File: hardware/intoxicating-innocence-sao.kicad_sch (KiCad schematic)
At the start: 0 parts

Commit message: Create board schematic
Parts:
- added C1: 100nF, Capacitor_SMD:C_0603_1608Metric_Pad1.08x0.95mm_HandSolder, symbol Device:C
- added D1, D2, D3: RED, LED_THT:LED_D3.0mm, symbol Device:LED
- added J1: SAO, kantoniak-kicad:SAO_Header_Addon_Side, symbol kantoniak-kicad:Conn_SAO
- added J2: QWIIC, Connector_JST:JST_SH_SM04B-SRSS-TB_1x04-1MP_P1.00mm_Horizontal, symbol kantoniak-kicad:QWIIC
- added R1, R10, R2, R8, R9: 10k, Resistor_SMD:R_0603_1608Metric_Pad0.98x0.95mm_HandSolder, symbol Device:R
- added R3, R4, R5, R6, R7: 330, Resistor_SMD:R_0603_1608Metric_Pad0.98x0.95mm_HandSolder, symbol Device:R
- added TP1: 3V3, TestPoint:TestPoint_Pad_D1.5mm, symbol Connector:TestPoint
- added TP2: GND, TestPoint:TestPoint_Pad_D1.5mm, symbol Connector:TestPoint
- added TP3: SWIO, TestPoint:TestPoint_Pad_D1.5mm, symbol Connector:TestPoint
- added TP4: ~{RST}, TestPoint:TestPoint_Pad_D1.5mm, symbol Connector:TestPoint
- added TP5: TXD, TestPoint:TestPoint_Pad_D1.5mm, symbol Connector:TestPoint
- added TP6: RXD, TestPoint:TestPoint_Pad_D1.5mm, symbol Connector:TestPoint
- added U1: CH32V003F4P6, Package_SO:TSSOP-20_4.4x6.5mm_P0.65mm, symbol MCU_WCH_RiscV:CH32V003FxPx
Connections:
- new net: D1.2 (A), R5.1
- new net: D2.2 (A), R6.1
- new net: D3.2 (A), R7.1
- new net: R4.2, U1.3 (PD6)
- new net: R3.1, U1.2 (PD5)
- new net +3V3: C1.1, J1.6 (3V3), J2.2 (3V3), R1.2, R2.2, TP1.1, U1.9 (VDD)
- new net CONFIG_A: R8.1, U1.17 (PC7)
- new net CONFIG_B: R9.2, U1.19 (PD2)
- new net CONFIG_C: R10.2, U1.20 (PD3)
- new net GND: C1.2, D1.1 (K), D2.1 (K), D3.1 (K), J1.1 (GND), J2.1 (GND), R10.1, R8.2, R9.1, TP2.1, U1.7 (VSS)
- new net LED_LEFT: R5.2, U1.13 (PC3)
- new net LED_RIGHT: R6.2, U1.14 (PC4)
- new net LED_TOP: R7.2, U1.15 (PC5)
- new net SCL: J1.2 (SCL), J2.3 (SDA), R2.1, U1.12 (PC2)
- new net SDA: J1.5 (SDA), J2.4 (SCL), R1.1, U1.11 (PC1)
- new net SWIO: TP3.1, U1.18 (PD1)
- new net UART_RX: R4.1, TP6.1
- new net UART_TX: R3.2, TP5.1
- new net ~{RST}: TP4.1, U1.4 (PD7)
- no-connect marks 0 -> 8
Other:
- note added: "Connectors"
- note added: "Extra configuration"
- note added: "LEDs - Eyes"

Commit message: Add bulk capacitor
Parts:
- added C1: 10uF, Capacitor_SMD:C_0603_1608Metric_Pad1.08x0.95mm_HandSolder, symbol Device:C
- renumbered C1 to C2
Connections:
- net +3V3: now also C1.1
- net GND: now also C1.2
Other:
- moved on the sheet: C2
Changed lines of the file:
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@@
 	)
 	(junction
+		(at 72.39 53.34)
+		(diameter 0)
+		(color 0 0 0 0)
+	)
+	(junction
 		(at 200.66 43.18)
 		(diameter 0)
@@
 	)
 	(junction
-		(at 82.55 30.48)
+		(at 81.28 30.48)
+		(diameter 0)
+		(color 0 0 0 0)
+	)
+	(junction
+		(at 72.39 30.48)
 		(diameter 0)
 		(color 0 0 0 0)
 	)
 	(junction
-		(at 82.55 53.34)
+		(at 81.28 53.34)
 		(diameter 0)
 		(color 0 0 0 0)
@@
 	(wire
 		(pts
+			(xy 72.39 30.48) (xy 72.39 38.1)
+		)
+		(stroke
+			(width 0)
+			(type default)
+		)
+	)
+	(wire
+		(pts
 			(xy 110.49 57.15) (xy 120.65 57.15)
 		)
@@
 	(wire
 		(pts
+			(xy 72.39 30.48) (xy 90.17 30.48)
+		)
+		(stroke
+			(width 0)
+			(type default)
+		)
+	)
+	(wire
+		(pts
 			(xy 45.72 48.26) (xy 45.72 53.34)
 		)
@@
 	(wire
 		(pts
-			(xy 82.55 53.34) (xy 82.55 55.88)
+			(xy 81.28 53.34) (xy 81.28 55.88)
 		)
 		(stroke
@@
 	(wire
 		(pts
-			(xy 82.55 30.48) (xy 82.55 38.1)
+			(xy 90.17 30.48) (xy 90.17 38.1)
 		)
 		(stroke
@@
 	(wire
 		(pts
-			(xy 41.91 40.64) (xy 59.69 40.64)
+			(xy 41.91 40.64) (xy 49.53 40.64)
+		)
+		(stroke
+			(width 0)
+			(type default)
+		)
+	)
+	(wire
+		(pts
+			(xy 41.91 38.1) (xy 49.53 38.1)
 		)
 		(stroke
@@
 	(wire
 		(pts
-			(xy 41.91 38.1) (xy 59.69 38.1)
+			(xy 72.39 53.34) (xy 90.17 53.34)
 		)
 		(stroke
@@
 	(wire
 		(pts
-			(xy 82.55 53.34) (xy 45.72 53.34)
+			(xy 72.39 45.72) (xy 72.39 53.34)
+		)
+		(stroke
+			(width 0)
+			(type default)
+		)
+	)
+	(wire
+		(pts
+			(xy 45.72 53.34) (xy 72.39 53.34)
 		)
 		(stroke
@@
 	(wire
 		(pts
-			(xy 82.55 27.94) (xy 82.55 30.48)
+			(xy 81.28 27.94) (xy 81.28 30.48)
 		)
 		(stroke
@@
 	(wire
 		(pts
-			(xy 45.72 30.48) (xy 82.55 30.48)
+			(xy 45.72 30.48) (xy 72.39 30.48)
 		)
 		(stroke
@@
 	(wire
 		(pts
-			(xy 82.55 45.72) (xy 82.55 53.34)
+			(xy 90.17 45.72) (xy 90.17 53.34)
 		)
 		(stroke
@@
 	(global_label "SDA"
 		(shape bidirectional)
-		(at 59.69 40.64 0)
+		(at 49.53 40.64 0)
 		(fields_autoplaced yes)
 		(effects
@@
 		)
 		(property "Intersheetrefs" "${INTERSHEET_REFS}"
-			(at 67.3546 40.64 0)
+			(at 57.1946 40.64 0)
 			(hide yes)
 			(show_name no)
@@
 	(global_label "SCL"
 		(shape output)
-		(at 59.69 38.1 0)
+		(at 49.53 38.1 0)
 		(fields_autoplaced yes)
 		(effects
@@
 		)
 		(property "Intersheetrefs" "${INTERSHEET_REFS}"
-			(at 66.1828 38.1 0)
+			(at 56.0228 38.1 0)
 			(hide yes)
 			(show_name no)
@@
 	)
 	(symbol
+		(lib_id "Device:C")
+		(at 72.39 41.91 0)
+		(unit 1)
+		(body_style 1)
+		(exclude_from_sim no)
+		(in_bom yes)
+		(on_board yes)
+		(in_pos_files yes)
+		(dnp no)
+		(fields_autoplaced yes)
+		(property "Reference" "C1"
+			(at 76.2 40.6399 0)
+			(show_name no)
+			(do_not_autoplace no)
+			(effects
+				(font
+					(size 1.27 1.27)
+				)
+				(justify left)
+			)
+		)
+		(property "Value" "10uF"
+			(at 76.2 43.1799 0)
+			(show_name no)
+			(do_not_autoplace no)
+			(effects
+				(font
+					(size 1.27 1.27)
+				)
+				(justify left)
+			)
+		)
+		(property "Footprint" "Capacitor_SMD:C_0603_1608Metric_Pad1.08x0.95mm_HandSolder"
+			(at 73.3552 45.72 0)
+			(hide yes)
+			(show_name no)
+			(do_not_autoplace no)
+			(effects
+				(font
+					(size 1.27 1.27)
+				)
+			)
+		)
+		(property "Datasheet" ""
+			(at 72.39 41.91 0)
+			(hide yes)
+			(show_name no)
+			(do_not_autoplace no)
+			(effects
+				(font
+					(size 1.27 1.27)
+				)
+			)
+		)
+		(property "Description" "Unpolarized capacitor"
+			(at 72.39 41.91 0)
+			(hide yes)
+			(show_name no)
+			(do_not_autoplace no)
+			(effects
+				(font
+					(size 1.27 1.27)
+				)
+			)
+		)
+		(property "LCSC Part #" "C109455"
+			(at 72.39 41.91 0)
+			(hide yes)
+			(show_name no)
+			(do_not_autoplace no)
+			(effects
+				(font
+					(size 1.27 1.27)
+				)
+			)
+		)
+		(pin "1"
+		)
+		(pin "2"
+		)
+		(instances
+			(project "intoxicating-innocence-sao"
+				(path "/559a265e-8809-44d3-9227-9bc29ae1c837"
+					(reference "C1")
+					(unit 1)
+				)
+			)
+		)
+	)
+	(symbol
 		(lib_id "Device:R")
 		(at 250.19 35.56 90)
@@
 	(symbol
 		(lib_id "Device:C")
-		(at 82.55 41.91 0)
+		(at 90.17 41.91 0)
 		(unit 1)
 		(body_style 1)
@@
 		(dnp no)
 		(fields_autoplaced yes)
-		(property "Reference" "C1"
-			(at 86.36 40.6399 0)
+		(property "Reference" "C2"
+			(at 93.98 40.6399 0)
 			(show_name no)
 			(do_not_autoplace no)
@@
 		)
 		(property "Value" "100nF"
-			(at 86.36 43.1799 0)
+			(at 93.98 43.1799 0)
 			(show_name no)
 			(do_not_autoplace no)
@@
 		)
 		(property "Footprint" "Capacitor_SMD:C_0603_1608Metric_Pad1.08x0.95mm_HandSolder"
-			(at 83.5152 45.72 0)
+			(at 91.1352 45.72 0)
 			(hide yes)
 			(show_name no)
@@
 		)
 		(property "Datasheet" ""
-			(at 82.55 41.91 0)
+			(at 90.17 41.91 0)
 			(hide yes)
 			(show_name no)
@@
 		)
 		(property "Description" "Unpolarized capacitor"
-			(at 82.55 41.91 0)
+			(at 90.17 41.91 0)
 			(hide yes)
 			(show_name no)
@@
 		)
 		(property "LCSC Part #" "C14663"
-			(at 82.55 41.91 0)
+			(at 90.17 41.91 0)
 			(hide yes)
 			(show_name no)
@@
 			(project "intoxicating-innocence-sao"
 				(path "/559a265e-8809-44d3-9227-9bc29ae1c837"
-					(reference "C1")
+					(reference "C2")
 					(unit 1)
 				)
@@
 	(symbol
 		(lib_id "power:+3V3")
-		(at 82.55 27.94 0)
+		(at 81.28 27.94 0)
 		(unit 1)
 		(body_style 1)
@@
 		(fields_autoplaced yes)
 		(property "Reference" "#PWR03"
-			(at 82.55 31.75 0)
+			(at 81.28 31.75 0)
 			(hide yes)
 			(show_name no)
@@
 		)
 		(property "Value" "+3V3"
-			(at 85.09 26.6699 0)
+			(at 83.82 26.6699 0)
 			(show_name no)
 			(do_not_autoplace no)
@@
 		)
 		(property "Footprint" ""
-			(at 82.55 27.94 0)
+			(at 81.28 27.94 0)
 			(hide yes)
 			(show_name no)
@@
 		)
 		(property "Datasheet" ""
-			(at 82.55 27.94 0)
+			(at 81.28 27.94 0)
 			(hide yes)
 			(show_name no)
@@
 		)
 		(property "Description" "Power symbol creates a global label with name \"+3V3\""
-			(at 82.55 27.94 0)
+			(at 81.28 27.94 0)
 			(hide yes)
 			(show_name no)
@@
 	(symbol
 		(lib_id "power:GND")
-		(at 82.55 55.88 0)
+		(at 81.28 55.88 0)
 		(unit 1)
 		(body_style 1)
@@
 		(fields_autoplaced yes)
 		(property "Reference" "#PWR04"
-			(at 82.55 62.23 0)
+			(at 81.28 62.23 0)
 			(hide yes)
 			(show_name no)
@@
 		)
 		(property "Value" "GND"
-			(at 85.09 57.1499 0)
+			(at 83.82 57.1499 0)
 			(show_name no)
 			(do_not_autoplace no)
@@
 		)
 		(property "Footprint" ""
-			(at 82.55 55.88 0)
+			(at 81.28 55.88 0)
 			(hide yes)
 			(show_name no)
@@
 		)
 		(property "Datasheet" ""
-			(at 82.55 55.88 0)
+			(at 81.28 55.88 0)
 			(hide yes)
 			(show_name no)
@@
 		)
 		(property "Description" "Power symbol creates a global label with name \"GND\" , ground"
-			(at 82.55 55.88 0)
+			(at 81.28 55.88 0)
 			(hide yes)
 			(show_name no)

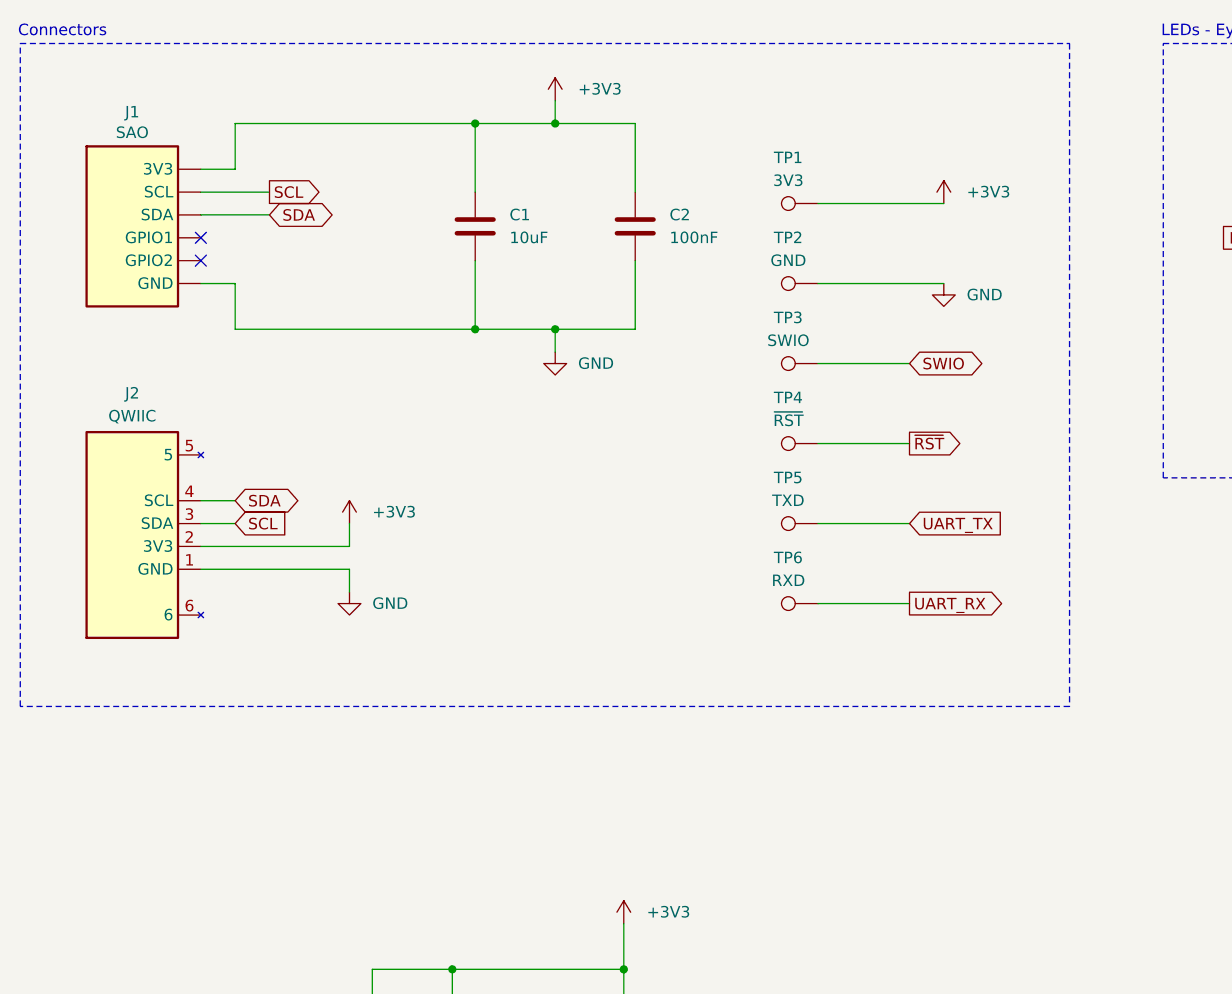
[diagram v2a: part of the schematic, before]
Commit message: Fix SCL/SDA routing, add I2C test pads
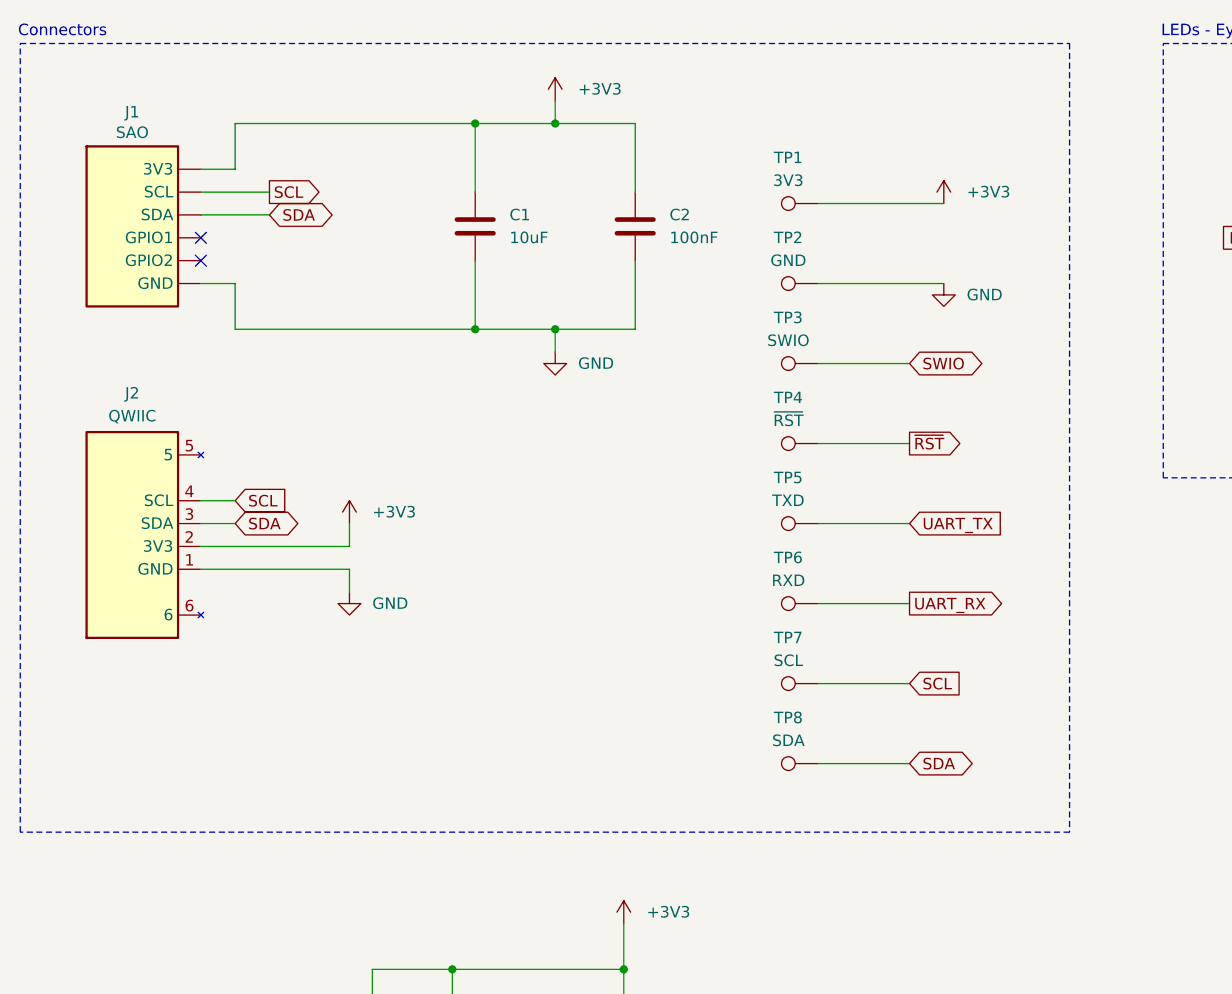
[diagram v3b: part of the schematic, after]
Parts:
- added TP7: SCL, TestPoint:TestPoint_Pad_D1.5mm, symbol Connector:TestPoint
- added TP8: SDA, TestPoint:TestPoint_Pad_D1.5mm, symbol Connector:TestPoint
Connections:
- net SCL: now also J2.4 (SCL), TP7.1; no longer J2.3 (SDA)
- net SDA: now also J2.3 (SDA), TP8.1; no longer J2.4 (SCL)
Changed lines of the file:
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@@
 	(rectangle
 		(start 21.844 21.59)
-		(end 138.43 95.25)
+		(end 138.43 109.22)
 		(stroke
 			(width 0)
@@
 	(wire
 		(pts
+			(xy 110.49 92.71) (xy 120.65 92.71)
+		)
+		(stroke
+			(width 0)
+			(type default)
+		)
+	)
+	(wire
+		(pts
+			(xy 110.49 101.6) (xy 120.65 101.6)
+		)
+		(stroke
+			(width 0)
+			(type default)
+		)
+	)
+	(wire
+		(pts
 			(xy 200.66 43.18) (xy 200.66 55.88)
 		)
@@
 		)
 	)
-	(global_label "SDA"
-		(shape bidirectional)
-		(at 45.72 72.39 0)
-		(fields_autoplaced yes)
-		(effects
-			(font
-				(size 1.27 1.27)
-			)
-			(justify left)
-		)
-		(property "Intersheetrefs" "${INTERSHEET_REFS}"
-			(at 53.3846 72.39 0)
-			(hide yes)
-			(show_name no)
-			(do_not_autoplace no)
-			(effects
-				(font
-					(size 1.27 1.27)
-				)
-				(justify left)
-			)
-		)
-	)
 	(global_label "LED_RIGHT"
 		(shape passive)
@@
 		)
 	)
+	(global_label "SCL"
+		(shape input)
+		(at 45.72 72.39 0)
+		(fields_autoplaced yes)
+		(effects
+			(font
+				(size 1.27 1.27)
+			)
+			(justify left)
+		)
+		(property "Intersheetrefs" "${INTERSHEET_REFS}"
+			(at 52.2128 72.39 0)
+			(hide yes)
+			(show_name no)
+			(do_not_autoplace no)
+			(effects
+				(font
+					(size 1.27 1.27)
+				)
+				(justify left)
+			)
+		)
+	)
 	(global_label "CONFIG_A"
 		(shape passive)
@@
 		)
 	)
+	(global_label "SCL"
+		(shape input)
+		(at 120.65 92.71 0)
+		(fields_autoplaced yes)
+		(effects
+			(font
+				(size 1.27 1.27)
+			)
+			(justify left)
+		)
+		(property "Intersheetrefs" "${INTERSHEET_REFS}"
+			(at 127.1428 92.71 0)
+			(hide yes)
+			(show_name no)
+			(do_not_autoplace no)
+			(effects
+				(font
+					(size 1.27 1.27)
+				)
+				(justify left)
+			)
+		)
+	)
 	(global_label "CONFIG_C"
 		(shape passive)
@@
 		)
 	)
+	(global_label "SDA"
+		(shape bidirectional)
+		(at 45.72 74.93 0)
+		(fields_autoplaced yes)
+		(effects
+			(font
+				(size 1.27 1.27)
+			)
+			(justify left)
+		)
+		(property "Intersheetrefs" "${INTERSHEET_REFS}"
+			(at 53.3846 74.93 0)
+			(hide yes)
+			(show_name no)
+			(do_not_autoplace no)
+			(effects
+				(font
+					(size 1.27 1.27)
+				)
+				(justify left)
+			)
+		)
+	)
 	(global_label "CONFIG_C"
 		(shape passive)
@@
 		)
 	)
-	(global_label "SCL"
-		(shape input)
-		(at 45.72 74.93 0)
+	(global_label "SDA"
+		(shape bidirectional)
+		(at 120.65 101.6 0)
 		(fields_autoplaced yes)
 		(effects
@@
 		)
 		(property "Intersheetrefs" "${INTERSHEET_REFS}"
-			(at 52.2128 74.93 0)
+			(at 128.3146 101.6 0)
 			(hide yes)
 			(show_name no)
@@
 				(path "/559a265e-8809-44d3-9227-9bc29ae1c837"
 					(reference "TP6")
+					(unit 1)
+				)
+			)
+		)
+	)
+	(symbol
+		(lib_id "Connector:TestPoint")
+		(at 110.49 101.6 90)
+		(unit 1)
+		(body_style 1)
+		(exclude_from_sim no)
+		(in_bom no)
+		(on_board yes)
+		(in_pos_files no)
+		(dnp no)
+		(fields_autoplaced yes)
+		(property "Reference" "TP8"
+			(at 107.188 96.52 90)
+			(show_name no)
+			(do_not_autoplace no)
+			(effects
+				(font
+					(size 1.27 1.27)
+				)
+			)
+		)
+		(property "Value" "SDA"
+			(at 107.188 99.06 90)
+			(show_name no)
+			(do_not_autoplace no)
+			(effects
+				(font
+					(size 1.27 1.27)
+				)
+			)
+		)
+		(property "Footprint" "TestPoint:TestPoint_Pad_D1.5mm"
+			(at 110.49 96.52 0)
+			(hide yes)
+			(show_name no)
+			(do_not_autoplace no)
+			(effects
+				(font
+					(size 1.27 1.27)
+				)
+			)
+		)
+		(property "Datasheet" ""
+			(at 110.49 96.52 0)
+			(hide yes)
+			(show_name no)
+			(do_not_autoplace no)
+			(effects
+				(font
+					(size 1.27 1.27)
+				)
+			)
+		)
+		(property "Description" "test point"
+			(at 110.49 101.6 0)
+			(hide yes)
+			(show_name no)
+			(do_not_autoplace no)
+			(effects
+				(font
+					(size 1.27 1.27)
+				)
+			)
+		)
+		(pin "1"
+		)
+		(instances
+			(project "intoxicating-innocence-sao"
+				(path "/559a265e-8809-44d3-9227-9bc29ae1c837"
+					(reference "TP8")
 					(unit 1)
 				)
@@
 					(unit 1)
 				)
+			)
+		)
+	)
+	(symbol
+		(lib_id "Connector:TestPoint")
+		(at 110.49 92.71 90)
+		(unit 1)
+		(body_style 1)
+		(exclude_from_sim no)
+		(in_bom no)
+		(on_board yes)
+		(in_pos_files no)
+		(dnp no)
+		(fields_autoplaced yes)
+		(property "Reference" "TP7"
+			(at 107.188 87.63 90)
+			(show_name no)
+			(do_not_autoplace no)
+			(effects
+				(font
+					(size 1.27 1.27)
+				)
+			)
+		)
+		(property "Value" "SCL"
+			(at 107.188 90.17 90)
+			(show_name no)
+			(do_not_autoplace no)
+			(effects
+				(font
+					(size 1.27 1.27)
+				)
+			)
+		)
+		(property "Footprint" "TestPoint:TestPoint_Pad_D1.5mm"
+			(at 110.49 87.63 0)
+			(hide yes)
+			(show_name no)
+			(do_not_autoplace no)
+			(effects
+				(font
+					(size 1.27 1.27)
+				)
+			)
+		)
+		(property "Datasheet" ""
+			(at 110.49 87.63 0)
+			(hide yes)
+			(show_name no)
+			(do_not_autoplace no)
+			(effects
+				(font
+					(size 1.27 1.27)
+				)
+			)
+		)
+		(property "Description" "test point"
+			(at 110.49 92.71 0)
+			(hide yes)
+			(show_name no)
+			(do_not_autoplace no)
+			(effects
+				(font
+					(size 1.27 1.27)
+				)
+			)
+		)
+		(pin "1"
+		)
+		(instances
+			(project "intoxicating-innocence-sao"
+				(path "/559a265e-8809-44d3-9227-9bc29ae1c837"
+					(reference "TP7")
+					(unit 1)
+				)
